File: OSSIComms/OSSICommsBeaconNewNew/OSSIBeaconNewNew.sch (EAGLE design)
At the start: 77 parts, among them Q1 NX-3215, U1 OPA2347, U2 MSP430F2132, U3 LM7321, U4 MAX1682, U5 MAX890L, U6 MAX4376, U7 TPS3838, U8 MCP1700_SOT23, X1 ESQ-126-38-G-D, X2 5268-03, X3 ICCON_POWERCON, X4 ICCON_POWERCON, X5 WEIDMULLER, X6 JTAG10PINMINI-H, X7 5268-03

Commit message: beacon newnew led new
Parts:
- removed JP2: (no value), OSSI:JP1Q
- removed LED3: (no value), SparkFun:LED0603
- removed Q1: NX-3215, OSSI:NX-3215
- removed R33: 1k, OSSI:R0603(1608)
- removed R63, R67: 250, OSSI:R0603(1608)
- removed R71: 10k, OSSI:R0603(1608)
- removed TP1, TP2, TP3, TP4, TP5, TP6, TP7: TP, OSSI:TP
- removed TR2: FDV301N, OSSI:FDV301N
- removed X6: JTAG10PINMINI-H, OSSI:JTAG10PINMINI-H
- removed X7: 5268-03, OSSI:5268-03
- added C13: 22nF, OSSI:C0603(1608)
- added C14: 1uF,0603, OSSI:C0603(1608)
- added C15: 100pF, OSSI:C0603(1608)
- added C16: 1uF 0805, OSSI:C0805(2012)
- added C19, C33: 1uF, OSSI:C0603(1608)
- added C20: (no value), OSSI:C0603(1608)
- added C21, C25: 1nF, OSSI:C0603(1608)
- added C22, C23, C24: 22pF, OSSI:C0603(1608)
- added C26, C31: 10nF, OSSI:C0603(1608)
- added C27: DNP, OSSI:C0603(1608)
- added C28: 22uF,1210, OSSI:C1210(3225)-GCM32
- added C29, C30: 10uF, LDO Tantal 16V, OSSI:C-TANTAL-A
- added C32, C34, C35, C36, C40, C42: 100nF, OSSI:C0603(1608)
- added C37, C41: TBD, OSSI:C0603(1608)
- added C38, C39: 12.5pF, OSSI:C0603(1608)
- added D1: BAT54S, OSSI:BAT54S
- added F1: LFCN-160, OSSI:LFCN-160
- added L1, L3: 470nH, 1008 size, OSSI:L1008(2502)
- added L2: 10nH, OSSI:L0603(1608)
- added L4, L5: 68nH, OSSI:L0603(1608)
- added L6: 5~15R ferrite bead, OSSI:L0805(2012)
- added Q2: NX-3215, OSSI:NX-3215
- added R26: 4.7k, OSSI:R0603(1608)
- added R27: 47k, OSSI:R0603(1608)
- added R28: 1M, OSSI:R0603(1608)
- added TCXO1: 19.2MHz, OSSI:TCXO-M532
- added U10: NC7SZ04, OSSI:NC7SZ04
- added U9: MAX6369, OSSI:MAX6369
- C1: value 1uF -> 100nF
- C10: value 100nF -> 1000pF
- C11: value 10uF, LDO Tantal 16V -> 22pF; device OSSI:C-TANTAL-A -> OSSI:C0603(1608)
- C12: value 10uF, LDO Tantal 16V -> 68pF; device OSSI:C-TANTAL-A -> OSSI:C0603(1608)
- C17: value 12.5pF -> 2.2uF, 0805; device OSSI:C0603(1608) -> OSSI:C0805(2012)
- C18: value 12.5pF -> 100pF
- C2: value 100nF -> 1uF
- C3: value 100nF -> 22uF,1210; device OSSI:C0603(1608) -> OSSI:C1210(3225)-GCM32
- C4: value 100nF -> 1uF,0805; device OSSI:C0603(1608) -> OSSI:C0805(2012)
- C6: value 10uF, LDO Tantal 16V -> 10nF; device OSSI:C-TANTAL-A -> OSSI:C0603(1608)
- C7: value 100nF -> 10nF
- C8: value 1uF 0805 -> 10nF; device OSSI:C0805(2012) -> OSSI:C0603(1608)
- C9: value 1206 Cap -> (none); device OSSI:C1206(3216)-GCM31 -> OSSI:C0603(1608)
- LED1: device led:LEDCHIPLED_0603 -> SparkFun:LED0603
- R1, R10: value TBD -> 100k
- R11: value 4.7k -> 23.7k
- R12, R8: value 4.7k -> 0
- R13: value 10k -> 4.7k
- R14: value 47k -> 4.7k
- R15, R17, R21: value (none) -> 100k
- R18: value 1k -> 4.7k
- R19: value (none) -> 4.7k
- R20: value (none) -> 10k
- R22: value 0.005, 2W RSENSE -> 250; device OSSI:RWSR2 -> OSSI:R0603(1608)
- R23: value 0 -> 1k
- R24: value 1.1k -> 10k
- R25: value 2.2k -> 250
- R3: value 100k -> 6.2k
- R4: value 1k -> 100k
- R5: value 100k -> 5.1k
- R6: value 100k -> 2.4k
- R7: value 1.5k -> 3.6k
- R9: value DNP -> 100k
- TR1: value FDD8896 -> FDV301N; device OSSI:FDD8896 -> OSSI:FDV301N
- U1: value OPA2347 -> MAX890L; device OSSI:OPA2347 -> OSSI:MAX890L
- U2: value MSP430F2132 -> ADL5530; device OSSI:MSP430F2132 -> OSSI:ADL5530
- U3: value LM7321 -> ADF7012; device OSSI:LM7321 -> OSSI:ADF7012
- U4: value MAX1682 -> MCP1700_SOT23; device OSSI:MAX1682 -> OSSI:MCP1700_SOT23
- U6: value MAX4376 -> TPS3838; device OSSI:MAX4376 -> OSSI:TPS3838
- U7: value TPS3838 -> OPA2347; device OSSI:TPS3838 -> OSSI:OPA2347
- U8: value MCP1700_SOT23 -> MSP430F2132; device OSSI:MCP1700_SOT23 -> OSSI:MSP430F2132
- X2: value 5268-03 -> RFCON-MCX-R/A; device OSSI:5268-03 -> OSSI:RFCON-MCX-R/A
- X3: value ICCON_POWERCON -> JTAG10PINMINI-H; device OSSI:ICCON_POWERCON -> OSSI:JTAG10PINMINI-H
- X4: value ICCON_POWERCON -> 5268-03; device OSSI:ICCON_POWERCON -> OSSI:5268-03
- X5: value WEIDMULLER -> 5268-02; device OSSI:WEIDMULLER -> OSSI:5268-02
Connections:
- removed net 3.3VLED: C10.1, C11.+, C2.1, C7.1, R10.1, R13.2, R2.2, R71.2, U1A.V+, U2.2, U6.P$3, U7.P$5, U8.2, X2.1, X6.4
- removed net ACLK_OUT: TP2.TP, U2.8
- removed net ADC2: U1B.-IN, U1B.OUT, U2.10
- removed net PWM: JP2.1, R19.2, R20.1
- removed net RESET_LED: R2.1, R8.2, U2.7, U7.P$4
- removed net SMCLK_OUT: TP1.TP, U2.25, X6.7
- removed net STRUT_GND: H1.MOUNT
- removed net SUN: R18.2, X2.2
- new net 3.3VBEACON: C28.1, C30.+, C31.1, C35.1, C36.1, D1.C2, L6.1, R1.2, R20.2, R24.2, R9.2, U4.2, U6.P$5, U7A.V+, U8.2, U9.P$4, U9.P$5, U9.P$6, U9.P$8, X3.4, X5.1
- new net ADC0: U7B.-IN, U7B.OUT, U8.8
- new net BEACON_CE: U3.CE, U8.18
- new net BEACON_CWCONTROL: R26.2, R27.1, X5.2
- new net BEACON_DATA: U3.TXDATA, U8.24
- new net BEACON_MUXOUT: U3.MUXOUT, U8.22
- new net BEACON_RFOUT: C24.2, C7.1, L5.2
- new net BEACON_SCLK: U3.CLK, U8.21
- new net BEACON_SDATA: U3.DATA, U8.20
- new net BEACON_SLE: U3.LE, U8.19
- new net BEACON_TXCLK: U3.TXCLK, U8.23
- new net BEACON_WDT_RST: C40.1, U6.P$3, U9.P$7
- new net N$1: R23.1, U8.11
- new net N$2: U8.27, X3.3
- new net N$34: C8.2, F1.P$1
- new net N$35: C9.1, F1.P$3
- new net N$36: C23.2, L4.2, L5.1
- new net N$37: C9.2, X2.1
- new net N$38: C25.2, C27.1, R28.2, U10.P$2
- new net N$40: C30.-, R12.1
- new net N$666: C29.+, C34.1, U4.3, U5.P$6, U5.P$7
- new net N$69: C25.1, TCXO1.P$3
- new net OSC1: C27.2, U3.OSC1
- new net OSC2: R28.1, U10.P$4, U3.OSC2
- new net PA_-FAULT: R1.1, U1.P$8, U8.3
- new net PA_ON: R4.2, TR1.G, U8.17
- new net RESETBEACON: R14.2, R9.1, U6.P$4, U8.7
- new net VBEACON_PA: C1.1, C3.1, C4.1, C5.1, C6.1, L1.1, U1.P$6, U1.P$7
- new net VCCRF: C14.1, C15.1, C20.1, C26.1, C32.1, L6.2, R8.1, TCXO1.P$4, U10.P$5, U3.DVDD_1
- net ADC1: now also U7A.-IN, U7A.OUT, U8.9; no longer U1A.-IN, U1A.OUT, U2.9
- net BEACON_-FAULT: now also U5.P$8
- net BEACON_OFF: now also C33.1, R10.2, U5.P$3
- net BEACON_SCL: now also R24.1, R25.1
- net BEACON_SDA: now also R20.1, R22.1
- net BUS_CS: now also R15.1
- net GND: now also C11.2, C12.1, C14.2, C15.2, C16.1, C17.1, C19.2, C20.2, C22.1, C23.1, C24.1, C26.2, C28.2, C29.-, C31.2, C32.2, C33.2, C34.2, C35.2, C36.2, C37.2, C38.2, C39.2, C40.2, C41.2, C42.2, C6.2, D1.A1, F1.P$2, F1.P$4, R10.1, R11.1, R12.2, R13.2, R16.2, R27.2, R4.1, R7.1, TCXO1.P$1, TCXO1.P$2, TR1.S, U1.P$4, U10.P$3, U2.1, U2.3, U2.5, U2.6, U2.8, U3.AGND, U3.DGND, U3.RFGND, U4.1, U6.P$1, U7A.V-, U8.4, U9.P$2, X2.2, X2.4, X2.5, X3.9, X4.1; no longer C10.2, C12.-, C17.2, C7.2, C8.2, C9.2, LED3.C, R1.1, R14.1, R17.2, R20.2, R23.2, R24.2, R25.1, R9.2, TP3.TP, TR2.S, U1A.V-, U3.V-, U4.P$1, U7.P$1, U7.P$2, U8.1, X4.P$1, X4.P$10, X4.P$2, X4.P$3, X4.P$4, X4.P$5, X4.P$6, X4.P$7, X4.P$8, X4.P$9, X5.2, X6.9, X7.1
- net LED_-FAULT: no longer U5.P$8
- net LED_OFF: no longer C1.1, R3.2, U5.P$3
- net LED_SCL: no longer R67.1, R71.1
- net LED_SDA: no longer R13.1, R63.1
- net N$10: now also R25.2, U8.13; no longer R1.2, U5.P$5
- net N$11: now also R18.2, U8.16; no longer R4.2, R5.2, R6.1
- net N$12: now also U8.10, U9.P$1; no longer R22.2, R7.1, TP6.TP, U6.P$5, X3.P$1, X3.P$10, X3.P$2, X3.P$3, X3.P$4, X3.P$5, X3.P$6, X3.P$7, X3.P$8, X3.P$9
- net N$13: now also C42.1, D1.C1A2, R26.1, U8.14; no longer C9.1, U3.V+, U4.P$2
- net N$14: now also L2.1, U3.L2; no longer R16.1, R25.2, U3.OUT
- net N$15: now also L2.2, U3.L1; no longer U2.27, X6.3
- net N$16: now also C13.1, C16.2, U3.CREG2; no longer R22.1, TP7.TP, TR1.S, U6.P$4
- net N$17: now also C13.2, U3.CVCO; no longer C11.-, R23.1
- net N$18: now also R7.2, U3.RSET; no longer R24.1, U3.-IN
- net N$19: now also C2.1, R2.1, TR1.D, U1.P$3; no longer C17.1, Q1.2, U2.5
- net N$20: now also C10.1, R6.1; no longer C18.1, Q1.1, U2.6
- net N$21: now also R3.2, U1.P$5; no longer JP1.2, LED3.A, R33.2
- net N$22: now also C41.1, R17.2, R21.1, U7B.+IN; no longer R63.2, U2.12
- net N$23: now also C21.2, L3.2, U3.RFOUT; no longer R67.2, U2.13
- net N$24: now also C11.1, R5.1, U3.VCOIN; no longer R15.1, U6.P$1
- net N$25: now also C17.2, U3.CREG1; no longer R33.1, U2.14
- net N$26: now also C10.2, C12.2, R5.2, U3.CPOUT; no longer C6.-, U4.P$3
- net N$27: now also C18.1, C19.1, L3.1, R8.2, U3.DVDD_2; no longer C6.+, U4.P$5
- net N$28: now also C7.2, U2.2; no longer R12.2, U2.16
- net N$29: now also C21.1, C22.2, L4.1; no longer LED1.A, R7.2
- net N$3: now also U8.26, X3.5; no longer U2.28, X6.1
- net N$30: now also C8.1, L1.2, U2.7; no longer R15.2, R17.1, TR2.G
- net N$31: now also R14.1, X3.10; no longer U2.26, X6.5
- net N$32: now also R11.2, U5.P$5; no longer R8.1, X6.10
- net N$33: now also C37.1, R15.2, R16.1, U7A.+IN; no longer JP2.2, U2.18
- net N$39: now also R19.2, U8.15; no longer R11.2, U2.15
- net N$4: now also U8.25, X3.7; no longer R10.2, U2.3
- net N$5: now also C38.1, Q2.2, U8.5; no longer C12.+, C3.1, U5.P$6, U5.P$7, U8.3
- net N$6: now also C39.1, Q2.1, U8.6; no longer R16.2, R9.1, TP5.TP, TR1.G, TR2.D
- net N$7: now also JP1.2, LED1.A, R23.2; no longer C4.1, R4.1, U1A.+IN
- net N$8: now also U8.28, X3.1; no longer C5.1, R18.1, U1B.+IN
- net N$9: now also R22.2, U8.12; no longer R19.1, R21.1, U3.+IN
- net RXD: now also R18.1, X4.3; no longer R12.1, X7.3
- net TEST: now also R13.1, U8.1, X3.8; no longer R14.2, U2.1, X6.8
- net TXD: now also R19.1, X4.2; no longer R11.1, X7.2
- net VBUS: now also R17.1, R2.2, U1.P$1, U1.P$2
- net VSUPERCAP: now also X1.13; no longer C8.1, R5.1, TP4.TP, TR1.D, U4.P$4, X5.1
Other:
- note added: "Capacitors!!!!!"
- note added: "Check TVS influences on OpAmp Input"
- note added: "Conntect Test Pin to JTAG!!"
- note added: "Current limited to 220mA"
- note added: "DIGITAL / RF POWER CHOKE"
- note added: "Max Current: 1.2A"
- note added: "PA Off by default"
- note added: "Pull Down resistor!!"
- note added: "Ref1: Poly Sat paper"
- note added: "Ref2: Pumpkin Co. Cubesat kit"
- note added: "current limited to 58.2mA"
- note added: "for SW connecting"
- note added: "use board's power"
- note removed: "10A - > 2.5V out from current sensor @ 0.005 R sense, @ G = 50"
- note removed: "Chagnge these 3 Resistor value to set the limit current!!!!!"
- note removed: "Check Supercap voltage!!!!!"
- note removed: "Cp out = 7.2V when Vsupercap = 3.6V"
- note removed: "Disconnect VSUPERCAP here as EPS provide measurement signal to OBC"
- note removed: "Expected Vgs = 3.6V"
- note removed: "Input protection needed when PWM ON, VSUPERCAP OFF"
- note removed: "Max VSupercap lmited to 3.6V by EPS"
- note removed: "Non-Inverting Amp, Gain ~ = 3"
- note removed: "set Current to 10A"

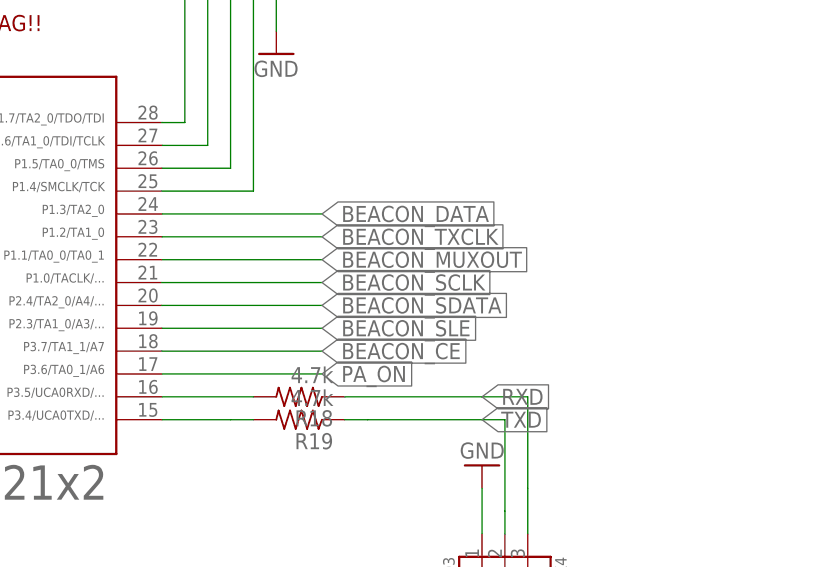
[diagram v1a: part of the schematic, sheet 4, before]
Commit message: series resistor added
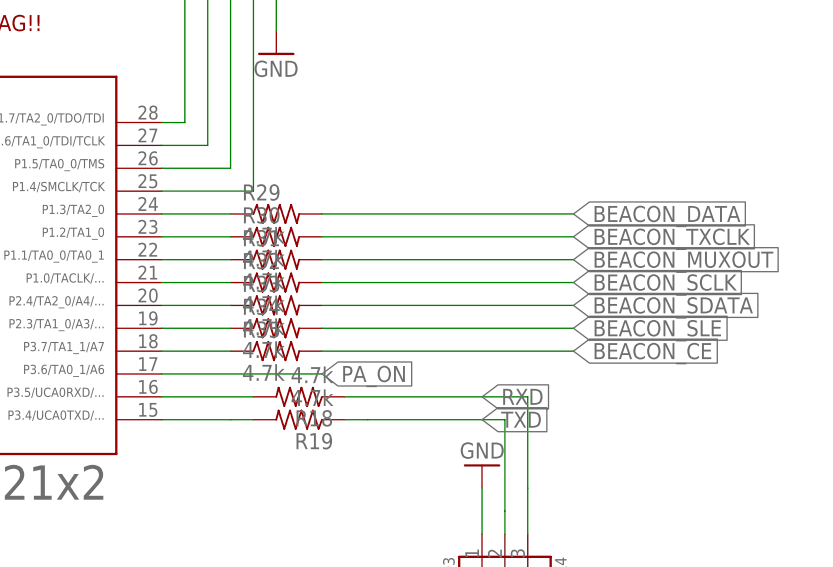
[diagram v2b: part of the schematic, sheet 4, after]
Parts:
- added R29, R30, R31, R32, R33, R34, R35: 4.7k, OSSI:R0603(1608)
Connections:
- new net N$41: R29.1, U8.24
- new net N$42: R30.1, U8.23
- new net N$43: R31.1, U8.22
- new net N$44: R32.1, U8.21
- new net N$45: R33.1, U8.20
- new net N$46: R34.1, U8.19
- new net N$47: R35.1, U8.18
- net BEACON_CE: now also R35.2; no longer U8.18
- net BEACON_DATA: now also R29.2; no longer U8.24
- net BEACON_MUXOUT: now also R31.2; no longer U8.22
- net BEACON_SCLK: now also R32.2; no longer U8.21
- net BEACON_SDATA: now also R33.2; no longer U8.20
- net BEACON_SLE: now also R34.2; no longer U8.19
- net BEACON_TXCLK: now also R30.2; no longer U8.23
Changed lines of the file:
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@@
 <part name="3.3VOBC5" library="OSSI" deviceset="3.3VBEACON" device=""/>
 <part name="C28" library="OSSI" deviceset="C" device="1210(3225)-GCM32" value="22uF,1210"/>
+<part name="R29" library="OSSI" deviceset="R" device="0603(1608)" value="4.7k"/>
+<part name="R30" library="OSSI" deviceset="R" device="0603(1608)" value="4.7k"/>
+<part name="R31" library="OSSI" deviceset="R" device="0603(1608)" value="4.7k"/>
+<part name="R32" library="OSSI" deviceset="R" device="0603(1608)" value="4.7k"/>
+<part name="R33" library="OSSI" deviceset="R" device="0603(1608)" value="4.7k"/>
+<part name="R34" library="OSSI" deviceset="R" device="0603(1608)" value="4.7k"/>
+<part name="R35" library="OSSI" deviceset="R" device="0603(1608)" value="4.7k"/>
 </parts>
 <sheets>
@@
 <instance part="3.3VOBC5" gate="G$1" x="208.28" y="66.04" rot="MR0"/>
 <instance part="C28" gate="G$1" x="294.64" y="226.06"/>
+<instance part="R29" gate="G$1" x="292.1" y="134.62"/>
+<instance part="R30" gate="G$1" x="292.1" y="132.08"/>
+<instance part="R31" gate="G$1" x="292.1" y="129.54"/>
+<instance part="R32" gate="G$1" x="292.1" y="127"/>
+<instance part="R33" gate="G$1" x="292.1" y="124.46"/>
+<instance part="R34" gate="G$1" x="292.1" y="121.92"/>
+<instance part="R35" gate="G$1" x="292.1" y="119.38"/>
 </instances>
 <busses>
@@
 <net name="BEACON_DATA" class="0">
 <segment>
-<pinref part="U8" gate="G$1" pin="24"/>
-<wire x1="279.4" y1="134.62" x2="297.18" y2="134.62" width="0.1524" layer="91"/>
-<label x="297.18" y="134.62" size="1.778" layer="95" xref="yes"/>
+<label x="325.12" y="134.62" size="1.778" layer="95" xref="yes"/>
+<pinref part="R29" gate="G$1" pin="2"/>
+<wire x1="297.18" y1="134.62" x2="325.12" y2="134.62" width="0.1524" layer="91"/>
 </segment>
 </net>
 <net name="BEACON_TXCLK" class="0">
 <segment>
-<pinref part="U8" gate="G$1" pin="23"/>
-<wire x1="279.4" y1="132.08" x2="297.18" y2="132.08" width="0.1524" layer="91"/>
-<label x="297.18" y="132.08" size="1.778" layer="95" xref="yes"/>
+<label x="325.12" y="132.08" size="1.778" layer="95" xref="yes"/>
+<pinref part="R30" gate="G$1" pin="2"/>
+<wire x1="297.18" y1="132.08" x2="325.12" y2="132.08" width="0.1524" layer="91"/>
 </segment>
 </net>
 <net name="BEACON_MUXOUT" class="0">
 <segment>
-<pinref part="U8" gate="G$1" pin="22"/>
-<wire x1="279.4" y1="129.54" x2="297.18" y2="129.54" width="0.1524" layer="91"/>
-<label x="297.18" y="129.54" size="1.778" layer="95" xref="yes"/>
+<label x="325.12" y="129.54" size="1.778" layer="95" xref="yes"/>
+<pinref part="R31" gate="G$1" pin="2"/>
+<wire x1="297.18" y1="129.54" x2="325.12" y2="129.54" width="0.1524" layer="91"/>
 </segment>
 </net>
 <net name="BEACON_SCLK" class="0">
 <segment>
-<pinref part="U8" gate="G$1" pin="21"/>
-<wire x1="279.4" y1="127" x2="297.18" y2="127" width="0.1524" layer="91"/>
-<label x="297.18" y="127" size="1.778" layer="95" xref="yes"/>
+<label x="325.12" y="127" size="1.778" layer="95" xref="yes"/>
+<pinref part="R32" gate="G$1" pin="2"/>
+<wire x1="297.18" y1="127" x2="325.12" y2="127" width="0.1524" layer="91"/>
 </segment>
 </net>
 <net name="BEACON_SDATA" class="0">
 <segment>
-<pinref part="U8" gate="G$1" pin="20"/>
-<wire x1="279.4" y1="124.46" x2="297.18" y2="124.46" width="0.1524" layer="91"/>
-<label x="297.18" y="124.46" size="1.778" layer="95" xref="yes"/>
+<label x="325.12" y="124.46" size="1.778" layer="95" xref="yes"/>
+<pinref part="R33" gate="G$1" pin="2"/>
+<wire x1="297.18" y1="124.46" x2="325.12" y2="124.46" width="0.1524" layer="91"/>
 </segment>
 </net>
 <net name="BEACON_SLE" class="0">
 <segment>
-<pinref part="U8" gate="G$1" pin="19"/>
-<wire x1="279.4" y1="121.92" x2="297.18" y2="121.92" width="0.1524" layer="91"/>
-<label x="297.18" y="121.92" size="1.778" layer="95" xref="yes"/>
+<label x="325.12" y="121.92" size="1.778" layer="95" xref="yes"/>
+<pinref part="R34" gate="G$1" pin="2"/>
+<wire x1="297.18" y1="121.92" x2="325.12" y2="121.92" width="0.1524" layer="91"/>
 </segment>
 </net>
 <net name="BEACON_CE" class="0">
 <segment>
-<pinref part="U8" gate="G$1" pin="18"/>
-<wire x1="279.4" y1="119.38" x2="297.18" y2="119.38" width="0.1524" layer="91"/>
-<label x="297.18" y="119.38" size="1.778" layer="95" xref="yes"/>
+<label x="325.12" y="119.38" size="1.778" layer="95" xref="yes"/>
+<pinref part="R35" gate="G$1" pin="2"/>
+<wire x1="297.18" y1="119.38" x2="325.12" y2="119.38" width="0.1524" layer="91"/>
 </segment>
 </net>
@@
 </segment>
 </net>
+<net name="N$41" class="0">
+<segment>
+<pinref part="U8" gate="G$1" pin="24"/>
+<pinref part="R29" gate="G$1" pin="1"/>
+<wire x1="279.4" y1="134.62" x2="287.02" y2="134.62" width="0.1524" layer="91"/>
+</segment>
+</net>
+<net name="N$42" class="0">
+<segment>
+<pinref part="U8" gate="G$1" pin="23"/>
+<pinref part="R30" gate="G$1" pin="1"/>
+<wire x1="279.4" y1="132.08" x2="287.02" y2="132.08" width="0.1524" layer="91"/>
+</segment>
+</net>
+<net name="N$43" class="0">
+<segment>
+<pinref part="U8" gate="G$1" pin="22"/>
+<pinref part="R31" gate="G$1" pin="1"/>
+<wire x1="279.4" y1="129.54" x2="287.02" y2="129.54" width="0.1524" layer="91"/>
+</segment>
+</net>
+<net name="N$44" class="0">
+<segment>
+<pinref part="U8" gate="G$1" pin="21"/>
+<pinref part="R32" gate="G$1" pin="1"/>
+<wire x1="279.4" y1="127" x2="287.02" y2="127" width="0.1524" layer="91"/>
+</segment>
+</net>
+<net name="N$45" class="0">
+<segment>
+<pinref part="U8" gate="G$1" pin="20"/>
+<pinref part="R33" gate="G$1" pin="1"/>
+<wire x1="279.4" y1="124.46" x2="287.02" y2="124.46" width="0.1524" layer="91"/>
+</segment>
+</net>
+<net name="N$46" class="0">
+<segment>
+<pinref part="U8" gate="G$1" pin="19"/>
+<pinref part="R34" gate="G$1" pin="1"/>
+<wire x1="279.4" y1="121.92" x2="287.02" y2="121.92" width="0.1524" layer="91"/>
+</segment>
+</net>
+<net name="N$47" class="0">
+<segment>
+<pinref part="U8" gate="G$1" pin="18"/>
+<pinref part="R35" gate="G$1" pin="1"/>
+<wire x1="279.4" y1="119.38" x2="287.02" y2="119.38" width="0.1524" layer="91"/>
+</segment>
+</net>

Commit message: beacon almost done
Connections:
- new net STRUT_GND: H1.MOUNT
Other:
- moved on the sheet: H1
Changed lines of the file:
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@@
 <instance part="VSOLAR4" gate="G$1" x="187.96" y="190.5"/>
 <instance part="STRUT_GND1" gate="G$1" x="195.58" y="91.44"/>
-<instance part="H1" gate="G$1" x="213.36" y="96.52"/>
+<instance part="H1" gate="G$1" x="215.9" y="96.52"/>
 <instance part="H2" gate="G$1" x="213.36" y="83.82"/>
 <instance part="H3" gate="G$1" x="213.36" y="71.12"/>
@@
 <pinref part="STRUT_GND1" gate="G$1" pin="STRUT_GND"/>
 <wire x1="213.36" y1="96.52" x2="195.58" y2="96.52" width="0.1524" layer="91"/>
-</segment>
-</net>
+<pinref part="H1" gate="G$1" pin="MOUNT"/>
+</segment>
+</net>

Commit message: gerber files are created / led current setting fixed to 9.7A
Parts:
- added C43: (no value), OSSI:C0805(2012)
- added R39: 511, OSSI:RWSL1206
- added TP1: TP, OSSI:TP
- added X6: (no value), OSSI:M03PTH
- added X7, X8: P-PAD-S, OSSI:P-PAD-S
- C1, C40, C5: value 100nF -> 10nF
- C10: value 1000pF -> 10nF
- C11, C22: value 22pF -> 1nF
- C12: value 68pF -> DNP
- C13: value 22nF -> 2.2uF, 0805; device OSSI:C0603(1608) -> OSSI:C0805(2012)
- C14: value 1uF,0603 -> 100pF
- C15: value 100pF -> 1uF,0603
- C16: value 1uF 0805 -> 68pF; device OSSI:C0805(2012) -> OSSI:C0603(1608)
- C17: value 2.2uF, 0805 -> 1000pF; device OSSI:C0805(2012) -> OSSI:C0603(1608)
- C18: value 100pF -> 1uF 0805; device OSSI:C0603(1608) -> OSSI:C0805(2012)
- C19: value 1uF -> 22pF
- C20: value (none) -> 22nF
- C21: value 1nF -> 100pF
- C23: value 22pF -> 1uF
- C25: value 1nF -> (none)
- C26: value 10nF -> 22pF
- C27: value DNP -> 22pF
- C28: value 22uF,1210 -> TBD; device OSSI:C1210(3225)-GCM32 -> OSSI:C0603(1608)
- C29: value 10uF, LDO Tantal 16V -> TBD; device OSSI:C-TANTAL-A -> OSSI:C0603(1608)
- C3: value 22uF,1210 -> 100nF; device OSSI:C1210(3225)-GCM32 -> OSSI:C0603(1608)
- C30: value 10uF, LDO Tantal 16V -> 100nF; device OSSI:C-TANTAL-A -> OSSI:C0603(1608)
- C31: value 10nF -> 1uF
- C33: value 1uF -> 100nF
- C34, C35: value 100nF -> 10uF, LDO Tantal 16V; device OSSI:C0603(1608) -> OSSI:C-TANTAL-A
- C36: value 100nF -> 12.5pF
- C37: value TBD -> 12.5pF
- C38, C39: value 12.5pF -> 100nF
- C4: value 1uF,0805 -> 10nF; device OSSI:C0805(2012) -> OSSI:C0603(1608)
- C41: value TBD -> 22uF,1210; device OSSI:C0603(1608) -> OSSI:C1210(3225)-GCM32
- C6: value 10nF -> 100nF
- C7: value 10nF -> 1uF,0805; device OSSI:C0603(1608) -> OSSI:C0805(2012)
- C8: value 10nF -> 22uF,1210; device OSSI:C0603(1608) -> OSSI:C1210(3225)-GCM32
- R11: value 23.7k -> 100k
- R12: value 0 -> 100k
- R13, R14: value 4.7k -> 100k
- R15: value 100k -> 23.7k
- R16, R9: value 100k -> 0
- R17: value 100k -> 10k
- R18: value 4.7k -> 10k
- R19: value 4.7k -> 250
- R20: value 10k -> 250
- R21: value 100k -> 4.7k
- R22: value 250 -> 100k
- R24: value 10k -> 47k
- R25: value 250 -> 4.7k
- R27: value 47k -> 4.7k
- R28: value 1M -> 4.7k
- R3: value 6.2k -> 100k
- R4: value 100k -> 6.2k
- R5: value 5.1k -> 1M
- R7: value 3.6k -> 5.1k
- R8: value 0 -> 3.6k
- U10: value NC7SZ04 -> MSP430F2132; device OSSI:NC7SZ04 -> OSSI:MSP430F2132
- U3: value ADF7012 -> NC7SZ04; device OSSI:ADF7012 -> OSSI:NC7SZ04
- U4: value MCP1700_SOT23 -> ADF7012; device OSSI:MCP1700_SOT23 -> OSSI:ADF7012
- U5: value MAX890L -> OPA2347; device OSSI:MAX890L -> OSSI:OPA2347
- U6: value TPS3838 -> MAX890L; device OSSI:TPS3838 -> OSSI:MAX890L
- U7: value OPA2347 -> MAX6369; device OSSI:OPA2347 -> OSSI:MAX6369
- U8: value MSP430F2132 -> MCP1700_SOT23; device OSSI:MSP430F2132 -> OSSI:MCP1700_SOT23
- U9: value MAX6369 -> TPS3838; device OSSI:MAX6369 -> OSSI:TPS3838
- X3: value JTAG10PINMINI-H -> 5268-02; device OSSI:JTAG10PINMINI-H -> OSSI:5268-02
- X4: value 5268-03 -> JTAG10PINMINI-H; device OSSI:5268-03 -> OSSI:JTAG10PINMINI-H
- X5: value 5268-02 -> 5268-03; device OSSI:5268-02 -> OSSI:5268-03
- renumbered Q2 to Q1
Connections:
- net 3.3VBEACON: now also C30.1, C35.+, C38.1, C40.1, C41.1, R17.2, R18.2, R22.2, R3.2, U10.2, U5A.V+, U7.P$4, U7.P$5, U7.P$6, U7.P$8, X3.1, X4.4; no longer C28.1, C30.+, C31.1, C35.1, C36.1, R1.2, R20.2, R24.2, R9.2, U4.2, U6.P$5, U7A.V+, U9.P$4, U9.P$6, U9.P$8, X3.4, X5.1
- net ADC0: now also U10.8, U5B.-IN, U5B.OUT; no longer U7B.-IN, U7B.OUT, U8.8
- net ADC1: now also U10.9, U5A.-IN, U5A.OUT; no longer U7A.-IN, U7A.OUT, U8.9
- net BEACON_-FAULT: now also U6.P$8; no longer U5.P$8
- net BEACON_CE: now also R26.2, U4.CE; no longer R35.2, U3.CE
- net BEACON_CWCONTROL: now also R24.1, R25.2, X3.2; no longer R26.2, R27.1, X5.2
- net BEACON_DATA: now also R32.2, U4.TXDATA; no longer R29.2, U3.TXDATA
- net BEACON_MUXOUT: now also R30.2, U4.MUXOUT; no longer R31.2, U3.MUXOUT
- net BEACON_OFF: now also C31.1, R14.2, U6.P$3; no longer C33.1, R10.2, U5.P$3
- net BEACON_RFOUT: now also C1.1, C27.2; no longer C24.2, C7.1
- net BEACON_SCL: now also R17.1, R20.1, X6.2; no longer R24.1, R25.1
- net BEACON_SCLK: now also R29.2, U4.CLK; no longer R32.2, U3.CLK
- net BEACON_SDA: now also R18.1, R19.1, X6.1; no longer R20.1, R22.1
- net BEACON_SDATA: now also R28.2, U4.DATA; no longer R33.2, U3.DATA
- net BEACON_SLE: now also R27.2, U4.LE; no longer R34.2, U3.LE
- net BEACON_TXCLK: now also R31.2, U4.TXCLK; no longer R30.2, U3.TXCLK
- net BEACON_WDT_RST: now also C33.1, U7.P$7, U9.P$3; no longer C40.1, U6.P$3, U9.P$7
- net BUS_CS: now also R13.1; no longer R15.1
- net GND: now also C10.2, C13.1, C18.1, C21.2, C23.2, C25.2, C26.1, C27.1, C29.2, C30.2, C34.-, C43.2, C7.2, C8.2, R1.1, R10.2, R14.1, R15.1, R24.2, R39.1, R8.1, TP1.TP, U10.4, U3.P$3, U4.AGND, U4.DGND, U4.RFGND, U5A.V-, U6.P$4, U7.P$2, U8.1, U9.P$1, X4.9, X5.1, X6.3, X8.P$1; no longer C1.2, C11.2, C12.1, C17.1, C18.2, C20.2, C22.1, C23.1, C26.2, C29.-, C34.2, C35.2, C4.2, R10.1, R11.1, R13.2, R27.2, R3.1, R7.1, U10.P$3, U3.AGND, U3.DGND, U3.RFGND, U4.1, U5.P$4, U6.P$1, U6.P$2, U7A.V-, U8.4, X3.9, X4.1
- net N$1: now also U10.11; no longer U8.11
- net N$10: now also R20.2, U10.13; no longer R25.2, U8.13
- net N$11: now also R34.2, U10.16; no longer R18.2, U8.16
- net N$12: now also U10.10, U7.P$1; no longer U8.10, U9.P$1
- net N$13: now also C39.1, R25.1, U10.14; no longer C42.1, R26.1, U8.14
- net N$14: now also U4.L2; no longer U3.L2
- net N$15: now also U4.L1; no longer U3.L1
- net N$16: now also C18.2, C20.1, U4.CREG2; no longer C13.1, C16.2, U3.CREG2
- net N$17: now also C20.2, U4.CVCO; no longer C13.2, U3.CVCO
- net N$18: now also R8.2, U4.RSET; no longer R7.2, U3.RSET
- net N$2: now also U10.27, X4.3; no longer U8.27, X3.3
- net N$20: now also C17.1; no longer C10.1
- net N$21: now also R4.2; no longer R3.2
- net N$22: now also C28.1, R10.1, R11.2, U5B.+IN; no longer C41.1, R17.2, R21.1, U7B.+IN
- net N$23: now also C22.2, U4.RFOUT; no longer C21.2, U3.RFOUT
- net N$24: now also C19.1, R7.1, U4.VCOIN; no longer C11.1, R5.1, U3.VCOIN
- net N$25: now also C13.2, U4.CREG1; no longer C17.2, U3.CREG1
- net N$26: now also C16.2, C17.2, R7.2, U4.CPOUT; no longer C10.2, C12.2, R5.2, U3.CPOUT
- net N$27: now also C21.1, C23.1, R9.2, U4.DVDD_2; no longer C18.1, C19.1, R8.2, U3.DVDD_2
- net N$28: now also C1.2; no longer C7.2
- net N$29: now also C22.1, C24.2; no longer C21.1, C22.2
- net N$3: now also U10.26, X4.5; no longer U8.26, X3.5
- net N$30: now also C4.1; no longer C8.1
- net N$31: now also R35.1, X4.10; no longer R14.1, X3.10
- net N$32: now also R15.2, U6.P$5; no longer R11.2, U5.P$5
- net N$33: now also C29.1, R12.1, R13.2, U5A.+IN; no longer C37.1, R15.2, R16.1, U7A.+IN
- net N$34: now also C4.2; no longer C8.2
- net N$36: now also C26.2; no longer C23.2
- net N$38: now also C11.2, C12.1, R5.2, U3.P$2; no longer C25.2, C27.1, R28.2, U10.P$2
- net N$39: now also R33.2, U10.15; no longer R19.2, U8.15
- net N$4: now also U10.25, X4.7; no longer U8.25, X3.7
- net N$40: now also C35.-, R16.1; no longer C30.-, R12.1
- net N$41: now also R32.1, U10.24; no longer R29.1, U8.24
- net N$42: now also R31.1, U10.23; no longer R30.1, U8.23
- net N$43: now also R30.1, U10.22; no longer R31.1, U8.22
- net N$44: now also R29.1, U10.21; no longer R32.1, U8.21
- net N$45: now also R28.1, U10.20; no longer R33.1, U8.20
- net N$46: now also R27.1, U10.19; no longer R34.1, U8.19
- net N$47: now also R26.1, U10.18; no longer R35.1, U8.18
- net N$5: now also C37.1, U10.5; no longer C38.1, U8.5
- net N$6: now also C36.1, U10.6; no longer C39.1, U8.6
- net N$666: now also C32.1, C34.+, U6.P$6, U6.P$7, U8.3; no longer C29.+, C34.1, U4.3, U5.P$6, U5.P$7
- net N$69: now also C11.1; no longer C25.1
- net N$8: now also U10.28, X4.1; no longer U8.28, X3.1
- net N$9: now also R19.2, U10.12; no longer R22.2, U8.12
- net OSC1: now also C12.2, U4.OSC1; no longer C27.2, U3.OSC1
- net OSC2: now also R5.1, U3.P$4, U4.OSC2; no longer R28.1, U10.P$4, U3.OSC2
- net PA_-FAULT: now also R3.1, U10.3; no longer R1.1, U8.3
- net PA_ON: now also R1.2, U10.17; no longer R4.2, U8.17
- net RESETBEACON: now also R22.1, R35.2, U10.7, U9.P$4; no longer R14.2, R9.1, U6.P$4, U8.7
- net RXD: now also R34.1, X5.3; no longer R18.1, X4.3
- net STRUT_GND: now also C43.1, H4.MOUNT, R39.2; no longer H1.MOUNT
- net TEST: now also R21.1, U10.1, X4.8; no longer R13.1, U8.1, X3.8
- net TXD: now also R33.1, X5.2; no longer R19.1, X4.2
- net VBEACON_PA: now also C7.1, C8.1; no longer C1.1, C4.1
- net VBUS: now also R11.1, U6.P$1, U6.P$2, X7.P$1; no longer R17.1, U5.P$1, U5.P$2
- net VCCRF: now also C10.1, C25.1, C42.1, R9.1, U3.P$5, U4.DVDD_1; no longer C20.1, C26.1, C32.1, R8.1, U10.P$5, U3.DVDD_1
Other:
- note added: "Do Not Place Comp! Only for the EPS"
- moved on the sheet: C1, C10, C11, C12, C13, C14, C15, C16, C17, C18, C19, C20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
